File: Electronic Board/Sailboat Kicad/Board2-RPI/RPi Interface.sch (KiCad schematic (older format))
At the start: 0 parts

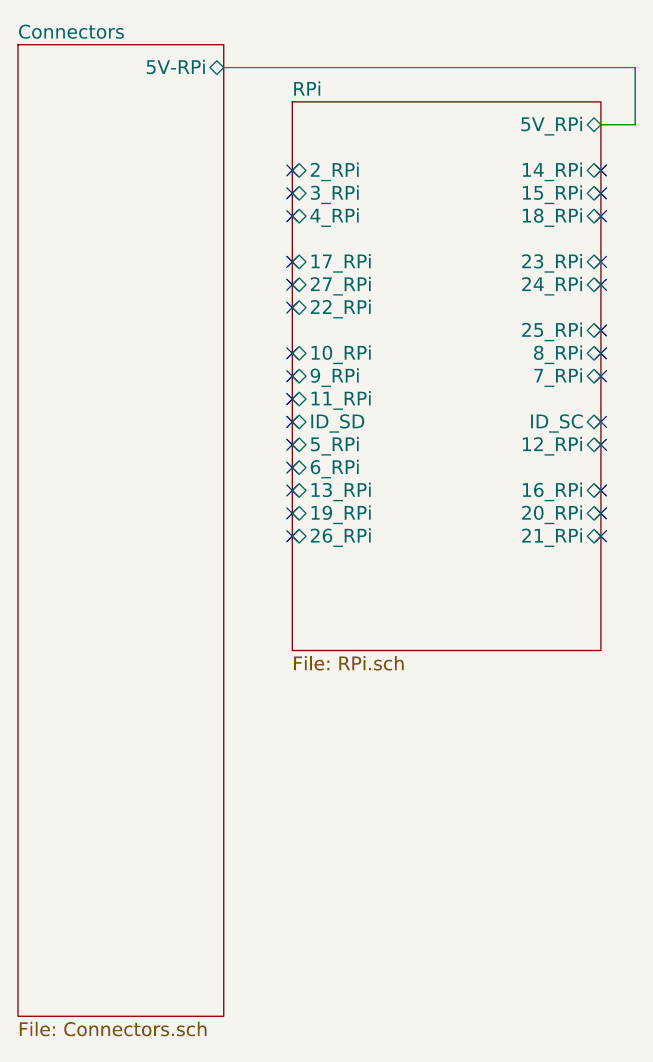
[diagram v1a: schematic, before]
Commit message: Cleaned up, and added security, text and better usability, preparation for board v2
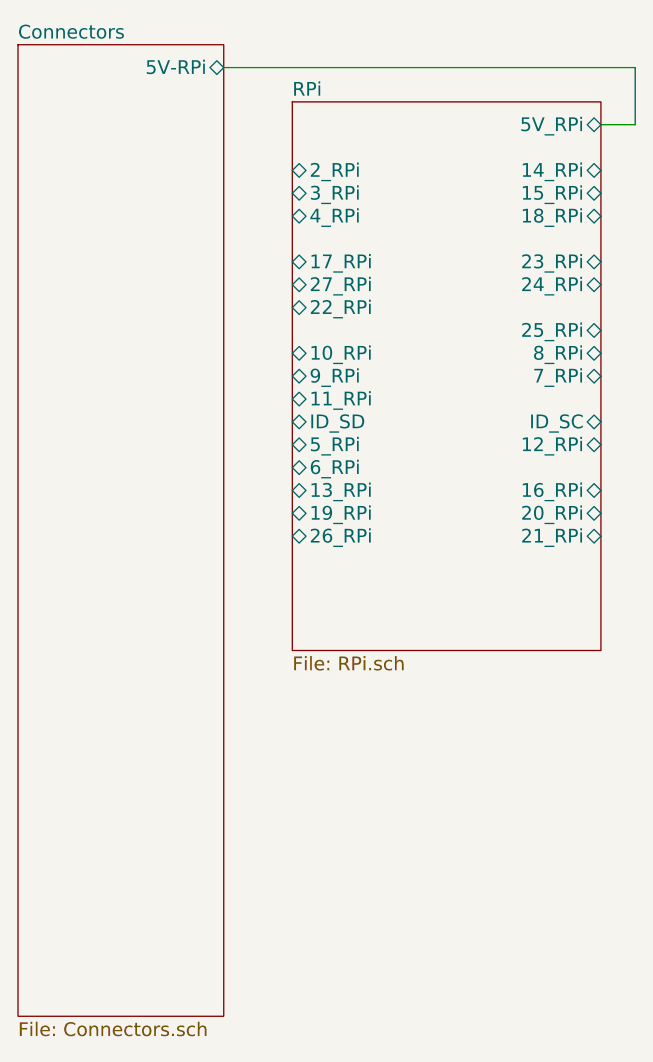
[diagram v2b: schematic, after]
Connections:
- no-connect marks 28 -> 0
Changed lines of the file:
@@
 Wire Wire Line
 	9200 900  9350 900
-NoConn ~ 9200 1100
-NoConn ~ 9200 1200
-NoConn ~ 9200 1300
-NoConn ~ 9200 1500
-NoConn ~ 9200 1600
-NoConn ~ 9200 1800
-NoConn ~ 9200 1900
-NoConn ~ 9200 2000
-NoConn ~ 7850 2100
-NoConn ~ 7850 2000
-NoConn ~ 7850 1900
-NoConn ~ 7850 1700
-NoConn ~ 7850 1600
-NoConn ~ 7850 1500
-NoConn ~ 7850 1300
-NoConn ~ 7850 1200
-NoConn ~ 7850 1100
-NoConn ~ 9200 2200
-NoConn ~ 9200 2300
-NoConn ~ 9200 2500
-NoConn ~ 9200 2600
-NoConn ~ 9200 2700
-NoConn ~ 7850 2700
-NoConn ~ 7850 2600
-NoConn ~ 7850 2500
-NoConn ~ 7850 2400
-NoConn ~ 7850 2300
-NoConn ~ 7850 2200
 $Sheet
 S 6650 550  900  4250
